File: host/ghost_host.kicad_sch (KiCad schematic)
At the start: 11 parts, among them J1 RGB_3_Pin_Connector, U9 kb2040

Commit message: finish host board v2 layout + production files
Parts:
- U9: now not fitted
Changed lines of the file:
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@@
 		(in_bom yes)
 		(on_board yes)
-		(dnp no)
+		(dnp yes)
 		(fields_autoplaced yes)
 		(property "Reference" "U9"

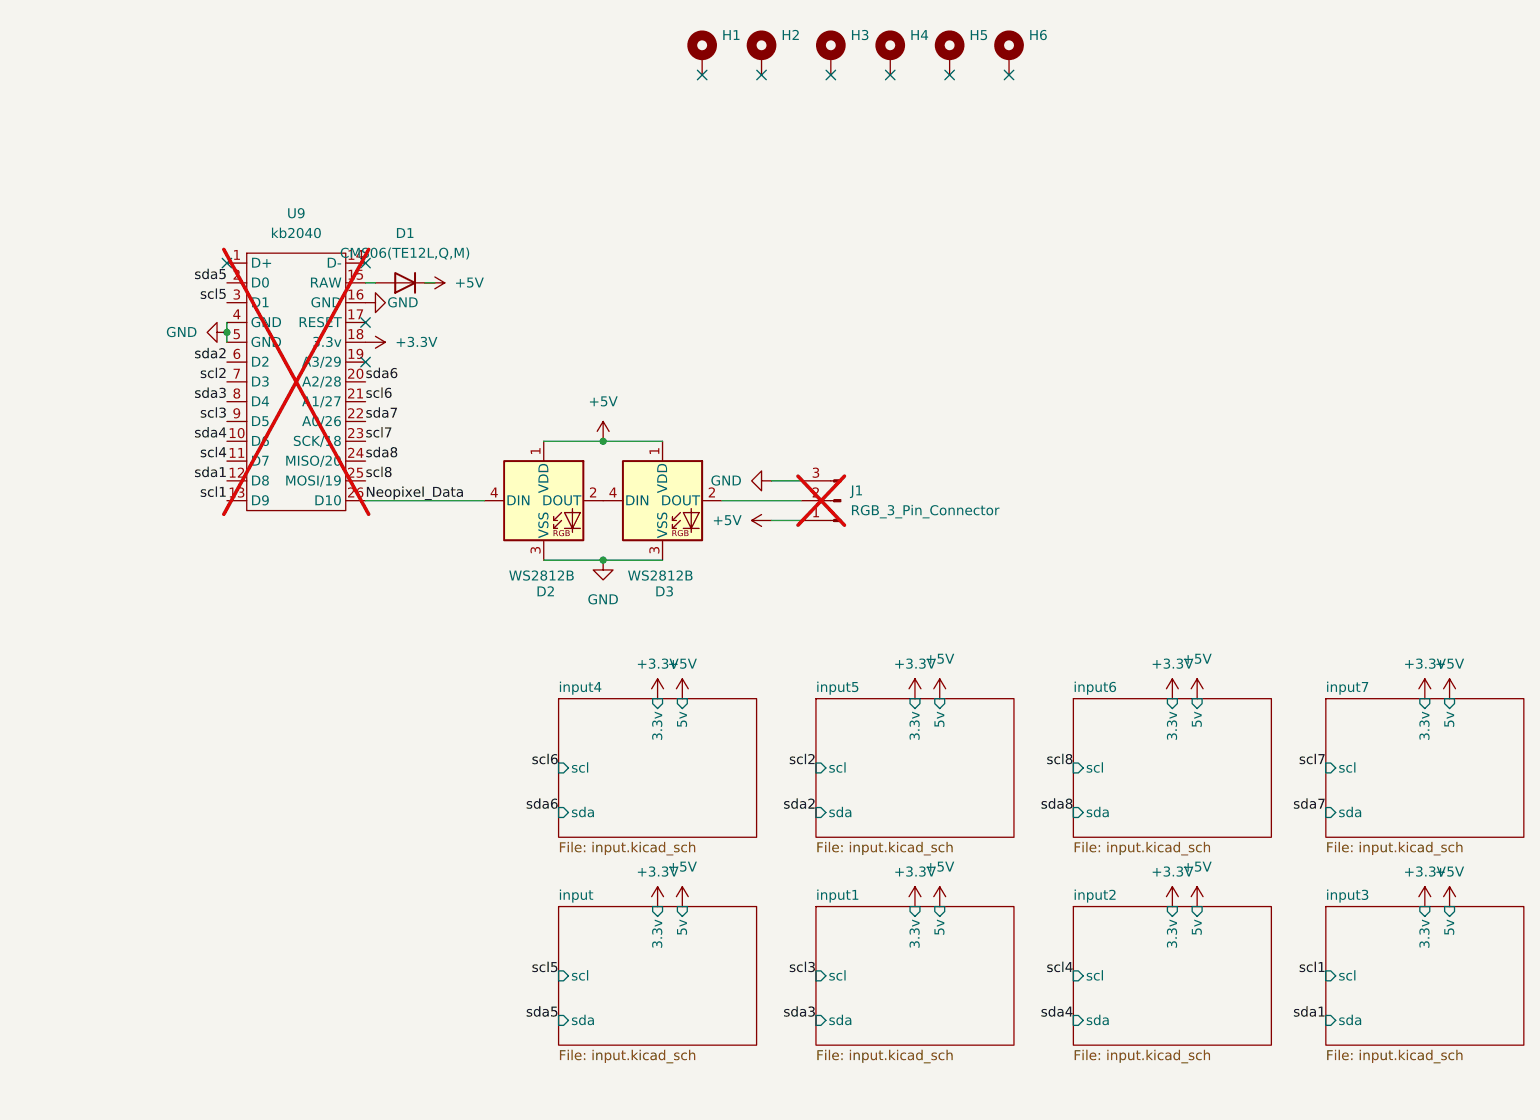
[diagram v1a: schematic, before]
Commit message: updated host schematic and imu production files
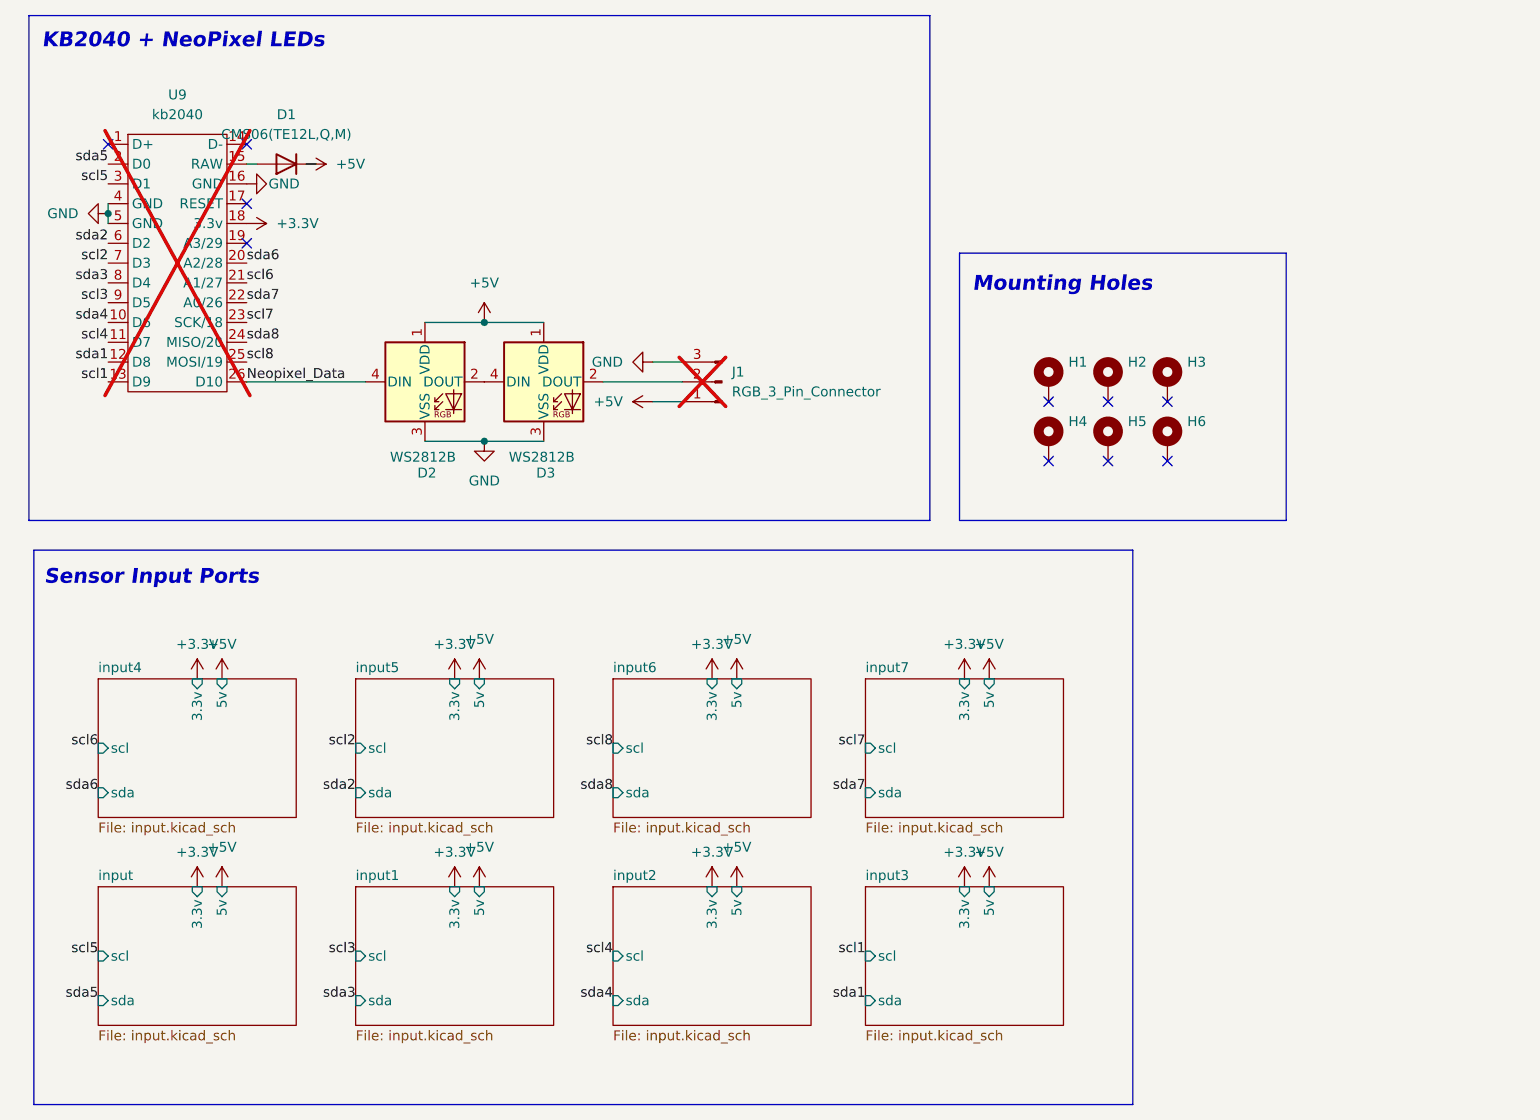
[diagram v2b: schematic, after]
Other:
- note added: "KB2040 + NeoPixel LEDs"
- note added: "Mounting Holes"
- note added: "Sensor Input Ports"
- moved on the sheet: D1, D2, D3, H1, H2, H3, H4, H5, H6, J1, U9
